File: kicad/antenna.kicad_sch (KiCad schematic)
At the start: 37 parts, among them J1 Bus_PCI_Express_x1, J4 Conn_01x02, J5 Conn_02x08_Odd_Even, J6 USB_C_Receptacle_USB2.0_16P, U2 RP2040, U4 W25Q128JVP, U9 MCP25625T-E/ML, X1 ABM8-272-T3, Y2 X322516MLB4SI

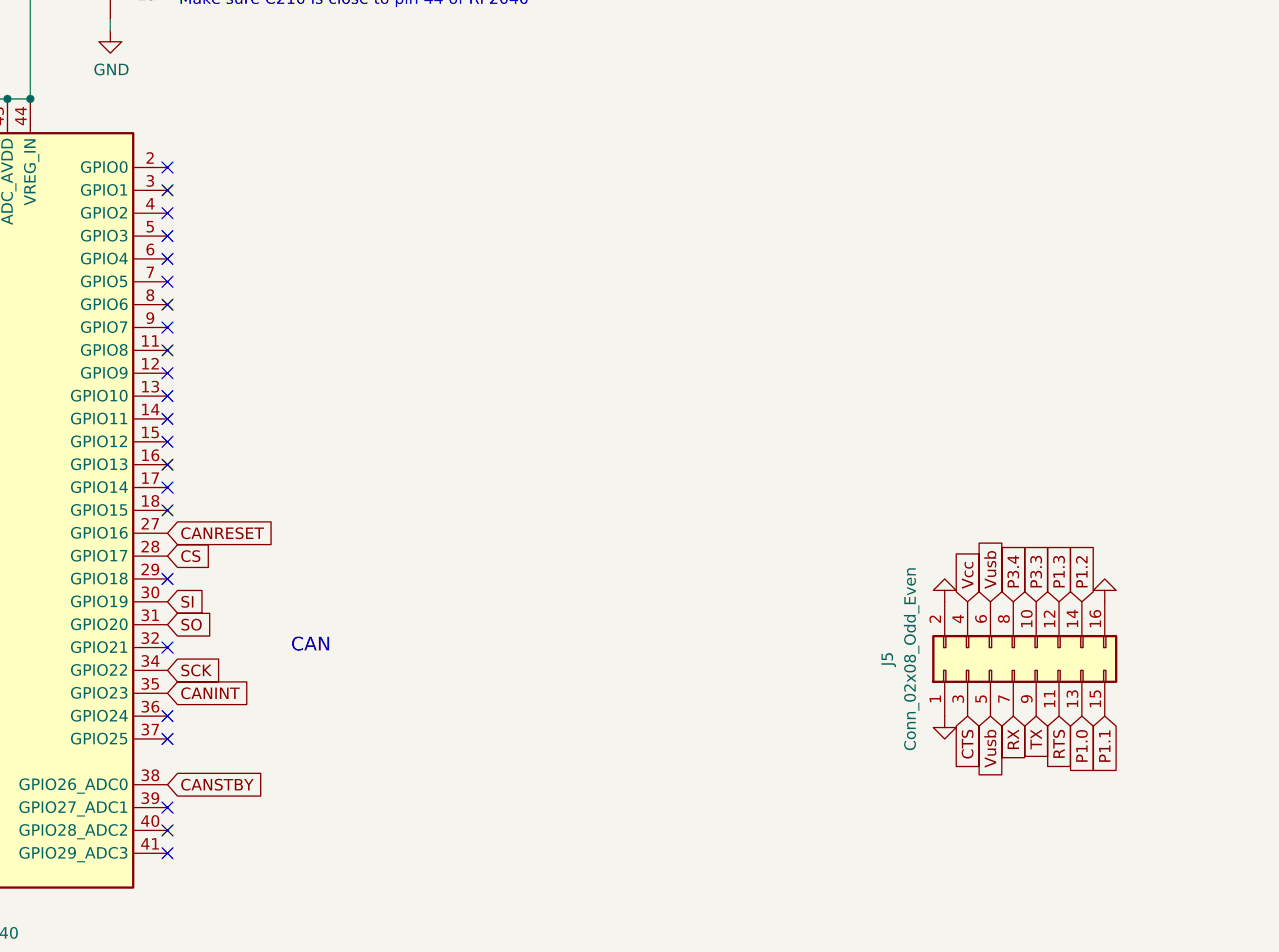
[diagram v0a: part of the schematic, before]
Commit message: update positioning of all chips to fit rfd900x
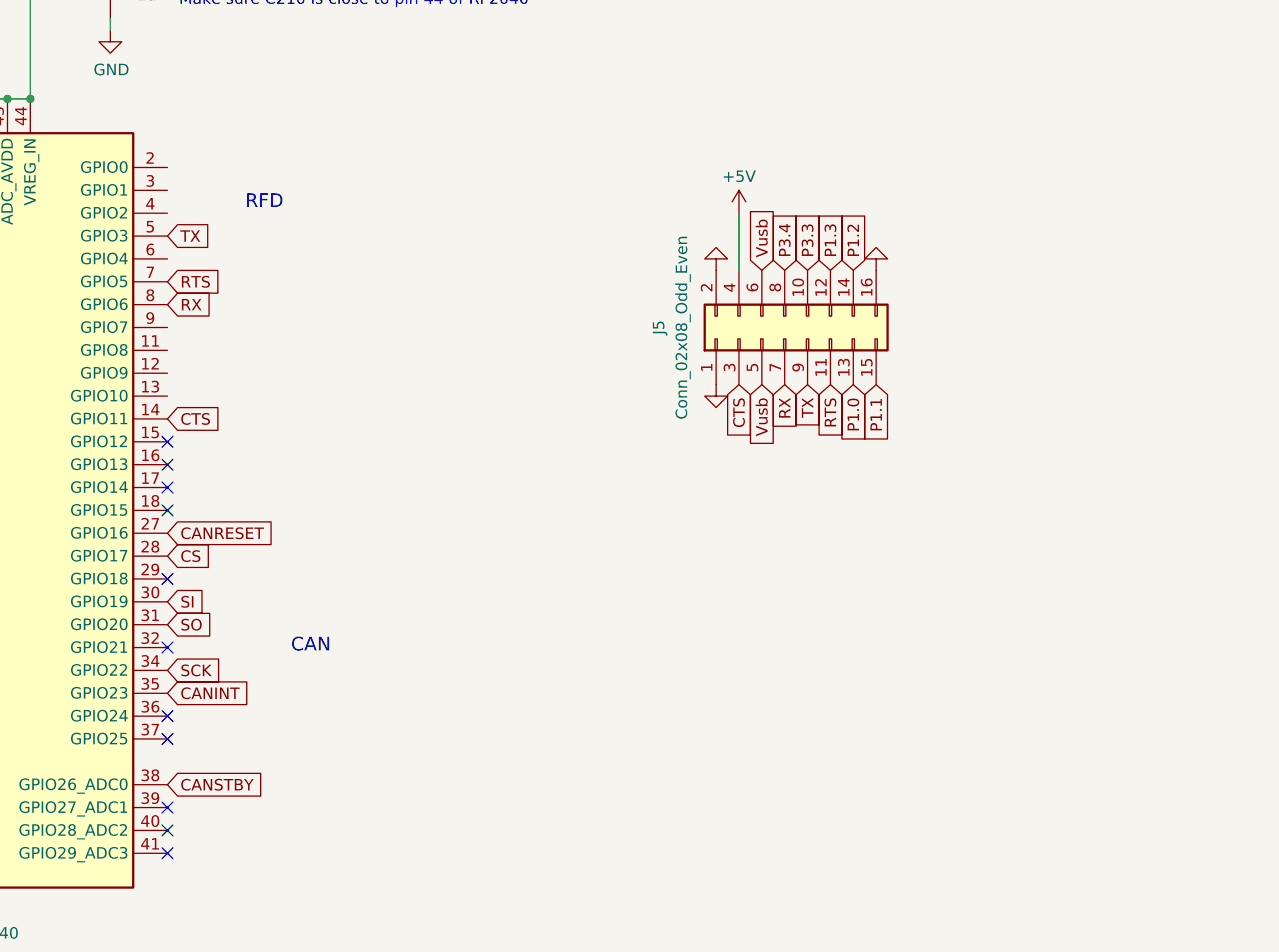
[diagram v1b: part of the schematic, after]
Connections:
- net Vcc is gone; now on net +5V: J5.4 (Pin_4)
- net CTS: now also U2.14 (GPIO11)
- net RTS: now also U2.7 (GPIO5)
- net RX: now also U2.8 (GPIO6)
- net TX: now also U2.5 (GPIO3)
- no-connect marks 43 -> 31
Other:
- note added: "RFD"
- moved on the sheet: J5

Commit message: test
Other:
- note added: "Antenna Module 0.1.0 test"
- note removed: "Antenna Module 0.1.0"
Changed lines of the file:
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@@
 		)
 	)
-	(text "Antenna Module 0.1.0"
+	(text "Antenna Module 0.1.0 test"
 		(exclude_from_sim no)
 		(at 493.014 386.842 0)
